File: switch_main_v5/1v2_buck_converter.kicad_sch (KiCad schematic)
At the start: 12 parts, among them U502 TPS62290TDRVRQ1

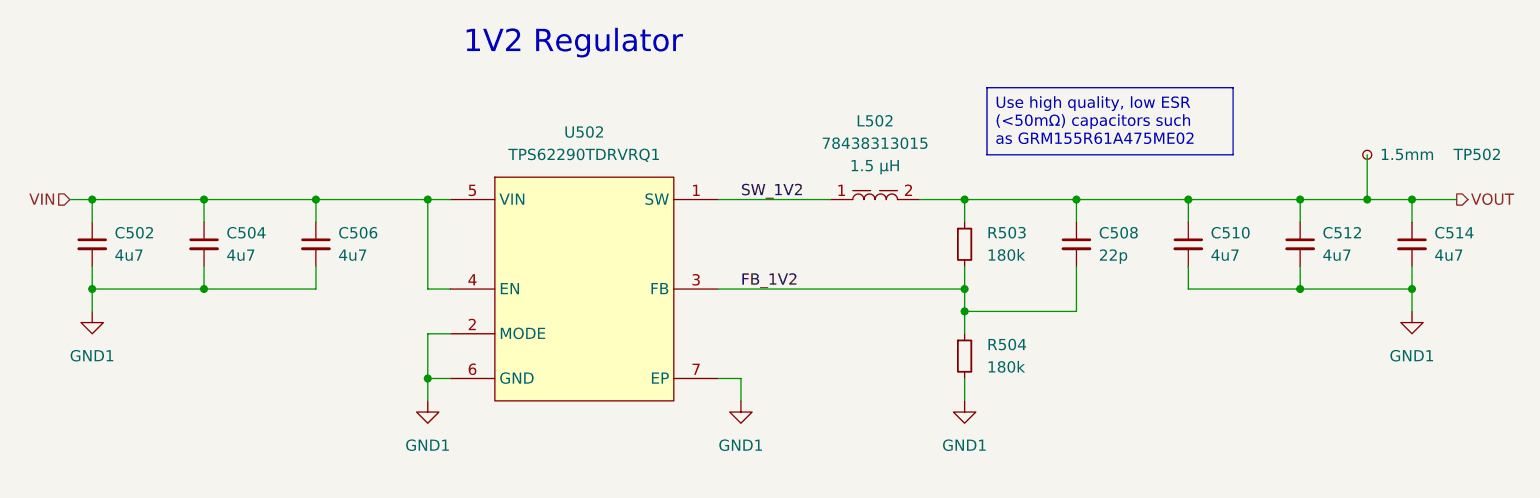
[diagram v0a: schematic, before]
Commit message: Updated 1v0_buck_converter feedback resistors
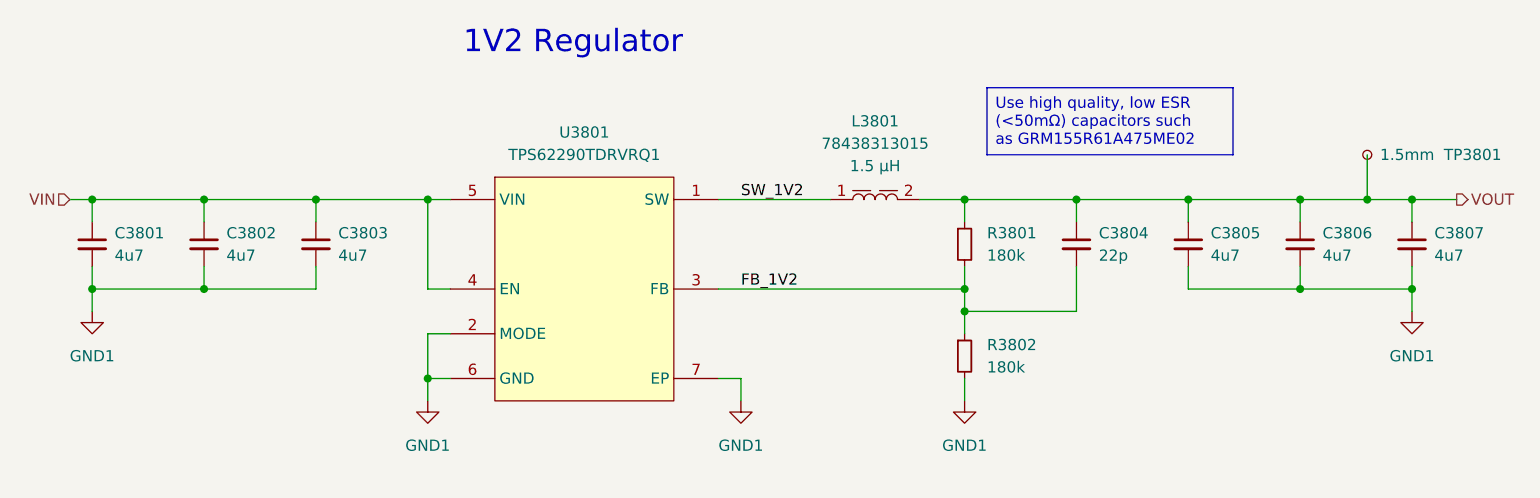
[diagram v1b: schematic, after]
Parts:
- renumbered C502 to C3801, C504 to C3802, C506 to C3803, C508 to C3804, C510 to C3805, C512 to C3806, C514 to C3807, L502 to L3801, R503 to R3801, R504 to R3802, TP502 to TP3801, U502 to U3801
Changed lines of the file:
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@@
 		(dnp no)
 		(fields_autoplaced yes)
-		(property "Reference" "C514"
+		(property "Reference" "C3807"
 			(at 231.14 95.2562 0)
 			(effects
@@
 			(project "switch_main_v5"
 				(path "/a5e57332-4284-4d3c-ab3c-13bc0ddb29b6/b1ff42f5-7cae-489e-9f8e-588cc93f3151/d017dddd-15df-4565-b589-89c8c78bc85c/6657ff67-3bc7-4183-a1c6-8c924b0e6f33"
-					(reference "C514")
+					(reference "C3807")
 					(unit 1)
 				)
@@
 		(dnp no)
 		(fields_autoplaced yes)
-		(property "Reference" "#PWR0514"
+		(property "Reference" "#PWR03805"
 			(at 228.6 110.49 0)
 			(effects
@@
 			(project "switch_main_v5"
 				(path "/a5e57332-4284-4d3c-ab3c-13bc0ddb29b6/b1ff42f5-7cae-489e-9f8e-588cc93f3151/d017dddd-15df-4565-b589-89c8c78bc85c/6657ff67-3bc7-4183-a1c6-8c924b0e6f33"
-					(reference "#PWR0514")
+					(reference "#PWR03805")
 					(unit 1)
 				)
@@
 		(dnp no)
 		(fields_autoplaced yes)
-		(property "Reference" "R504"
+		(property "Reference" "R3802"
 			(at 180.34 107.9499 0)
 			(effects
@@
 			(project "switch_main_v5"
 				(path "/a5e57332-4284-4d3c-ab3c-13bc0ddb29b6/b1ff42f5-7cae-489e-9f8e-588cc93f3151/d017dddd-15df-4565-b589-89c8c78bc85c/6657ff67-3bc7-4183-a1c6-8c924b0e6f33"
-					(reference "R504")
+					(reference "R3802")
 					(unit 1)
 				)
@@
 		(dnp no)
 		(fields_autoplaced yes)
-		(property "Reference" "C510"
+		(property "Reference" "C3805"
 			(at 205.74 95.2562 0)
 			(effects
@@
 			(project "switch_main_v5"
 				(path "/a5e57332-4284-4d3c-ab3c-13bc0ddb29b6/b1ff42f5-7cae-489e-9f8e-588cc93f3151/d017dddd-15df-4565-b589-89c8c78bc85c/6657ff67-3bc7-4183-a1c6-8c924b0e6f33"
-					(reference "C510")
+					(reference "C3805")
 					(unit 1)
 				)
@@
 		(dnp no)
 		(fields_autoplaced yes)
-		(property "Reference" "#PWR0506"
+		(property "Reference" "#PWR03802"
 			(at 116.84 120.65 0)
 			(effects
@@
 			(project "switch_main_v5"
 				(path "/a5e57332-4284-4d3c-ab3c-13bc0ddb29b6/b1ff42f5-7cae-489e-9f8e-588cc93f3151/d017dddd-15df-4565-b589-89c8c78bc85c/6657ff67-3bc7-4183-a1c6-8c924b0e6f33"
-					(reference "#PWR0506")
+					(reference "#PWR03802")
 					(unit 1)
 				)
@@
 		(on_board yes)
 		(dnp no)
-		(property "Reference" "C502"
+		(property "Reference" "C3801"
 			(at 81.28 95.2562 0)
 			(effects
@@
 			(project "switch_main_v5"
 				(path "/a5e57332-4284-4d3c-ab3c-13bc0ddb29b6/b1ff42f5-7cae-489e-9f8e-588cc93f3151/d017dddd-15df-4565-b589-89c8c78bc85c/6657ff67-3bc7-4183-a1c6-8c924b0e6f33"
-					(reference "C502")
+					(reference "C3801")
 					(unit 1)
 				)
@@
 		(on_board yes)
 		(dnp no)
-		(property "Reference" "C506"
+		(property "Reference" "C3803"
 			(at 106.68 95.2562 0)
 			(effects
@@
 			(project "switch_main_v5"
 				(path "/a5e57332-4284-4d3c-ab3c-13bc0ddb29b6/b1ff42f5-7cae-489e-9f8e-588cc93f3151/d017dddd-15df-4565-b589-89c8c78bc85c/6657ff67-3bc7-4183-a1c6-8c924b0e6f33"
-					(reference "C506")
+					(reference "C3803")
 					(unit 1)
 				)
@@
 		(dnp no)
 		(fields_autoplaced yes)
-		(property "Reference" "#PWR0510"
+		(property "Reference" "#PWR03804"
 			(at 177.8 120.65 0)
 			(effects
@@
 			(project "switch_main_v5"
 				(path "/a5e57332-4284-4d3c-ab3c-13bc0ddb29b6/b1ff42f5-7cae-489e-9f8e-588cc93f3151/d017dddd-15df-4565-b589-89c8c78bc85c/6657ff67-3bc7-4183-a1c6-8c924b0e6f33"
-					(reference "#PWR0510")
+					(reference "#PWR03804")
 					(unit 1)
 				)
@@
 		(on_board yes)
 		(dnp no)
-		(property "Reference" "C508"
+		(property "Reference" "C3804"
 			(at 193.04 95.2562 0)
 			(effects
@@
 			(project "switch_main_v5"
 				(path "/a5e57332-4284-4d3c-ab3c-13bc0ddb29b6/b1ff42f5-7cae-489e-9f8e-588cc93f3151/d017dddd-15df-4565-b589-89c8c78bc85c/6657ff67-3bc7-4183-a1c6-8c924b0e6f33"
-					(reference "C508")
+					(reference "C3804")
 					(unit 1)
 				)
@@
 		(dnp no)
 		(fields_autoplaced yes)
-		(property "Reference" "R503"
+		(property "Reference" "R3801"
 			(at 180.34 95.2499 0)
 			(effects
@@
 			(project "switch_main_v5"
 				(path "/a5e57332-4284-4d3c-ab3c-13bc0ddb29b6/b1ff42f5-7cae-489e-9f8e-588cc93f3151/d017dddd-15df-4565-b589-89c8c78bc85c/6657ff67-3bc7-4183-a1c6-8c924b0e6f33"
-					(reference "R503")
+					(reference "R3801")
 					(unit 1)
 				)
@@
 		(dnp no)
 		(fields_autoplaced yes)
-		(property "Reference" "C512"
+		(property "Reference" "C3806"
 			(at 218.44 95.2562 0)
 			(effects
@@
 			(project "switch_main_v5"
 				(path "/a5e57332-4284-4d3c-ab3c-13bc0ddb29b6/b1ff42f5-7cae-489e-9f8e-588cc93f3151/d017dddd-15df-4565-b589-89c8c78bc85c/6657ff67-3bc7-4183-a1c6-8c924b0e6f33"
-					(reference "C512")
+					(reference "C3806")
 					(unit 1)
 				)
@@
 		(dnp no)
 		(fields_autoplaced yes)
-		(property "Reference" "#PWR0504"
+		(property "Reference" "#PWR03801"
 			(at 78.74 110.49 0)
 			(effects
@@
 			(project "switch_main_v5"
 				(path "/a5e57332-4284-4d3c-ab3c-13bc0ddb29b6/b1ff42f5-7cae-489e-9f8e-588cc93f3151/d017dddd-15df-4565-b589-89c8c78bc85c/6657ff67-3bc7-4183-a1c6-8c924b0e6f33"
-					(reference "#PWR0504")
+					(reference "#PWR03801")
 					(unit 1)
 				)
@@
 		(dnp no)
 		(fields_autoplaced yes)
-		(property "Reference" "U502"
+		(property "Reference" "U3801"
 			(at 134.62 83.82 0)
 			(effects
@@
 			(project "switch_main_v5"
 				(path "/a5e57332-4284-4d3c-ab3c-13bc0ddb29b6/b1ff42f5-7cae-489e-9f8e-588cc93f3151/d017dddd-15df-4565-b589-89c8c78bc85c/6657ff67-3bc7-4183-a1c6-8c924b0e6f33"
-					(reference "U502")
+					(reference "U3801")
 					(unit 1)
 				)
@@
 		(dnp no)
 		(fields_autoplaced yes)
-		(property "Reference" "L502"
+		(property "Reference" "L3801"
 			(at 167.64 82.55 0)
 			(effects
@@
 			(project "switch_main_v5"
 				(path "/a5e57332-4284-4d3c-ab3c-13bc0ddb29b6/b1ff42f5-7cae-489e-9f8e-588cc93f3151/d017dddd-15df-4565-b589-89c8c78bc85c/6657ff67-3bc7-4183-a1c6-8c924b0e6f33"
-					(reference "L502")
+					(reference "L3801")
 					(unit 1)
 				)
@@
 		(dnp no)
 		(fields_autoplaced yes)
-		(property "Reference" "#PWR0508"
+		(property "Reference" "#PWR03803"
 			(at 152.4 120.65 0)
 			(effects
@@
 			(project "switch_main_v5"
 				(path "/a5e57332-4284-4d3c-ab3c-13bc0ddb29b6/b1ff42f5-7cae-489e-9f8e-588cc93f3151/d017dddd-15df-4565-b589-89c8c78bc85c/6657ff67-3bc7-4183-a1c6-8c924b0e6f33"
-					(reference "#PWR0508")
+					(reference "#PWR03803")
 					(unit 1)
 				)
@@
 		(on_board yes)
 		(dnp no)
-		(property "Reference" "C504"
+		(property "Reference" "C3802"
 			(at 93.98 95.2562 0)
 			(effects
@@
 			(project "switch_main_v5"
 				(path "/a5e57332-4284-4d3c-ab3c-13bc0ddb29b6/b1ff42f5-7cae-489e-9f8e-588cc93f3151/d017dddd-15df-4565-b589-89c8c78bc85c/6657ff67-3bc7-4183-a1c6-8c924b0e6f33"
-					(reference "C504")
+					(reference "C3802")
 					(unit 1)
 				)
@@
 		(on_board yes)
 		(dnp no)
-		(property "Reference" "TP502"
+		(property "Reference" "TP3801"
 			(at 238.76 86.36 0)
 			(effects
@@
 			(project "switch_main_v5"
 				(path "/a5e57332-4284-4d3c-ab3c-13bc0ddb29b6/b1ff42f5-7cae-489e-9f8e-588cc93f3151/d017dddd-15df-4565-b589-89c8c78bc85c/6657ff67-3bc7-4183-a1c6-8c924b0e6f33"
-					(reference "TP502")
-					(unit 1)
-				)
+					(reference "TP3801")
+					(unit 1)
+				)

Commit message: 1V0 Rail done
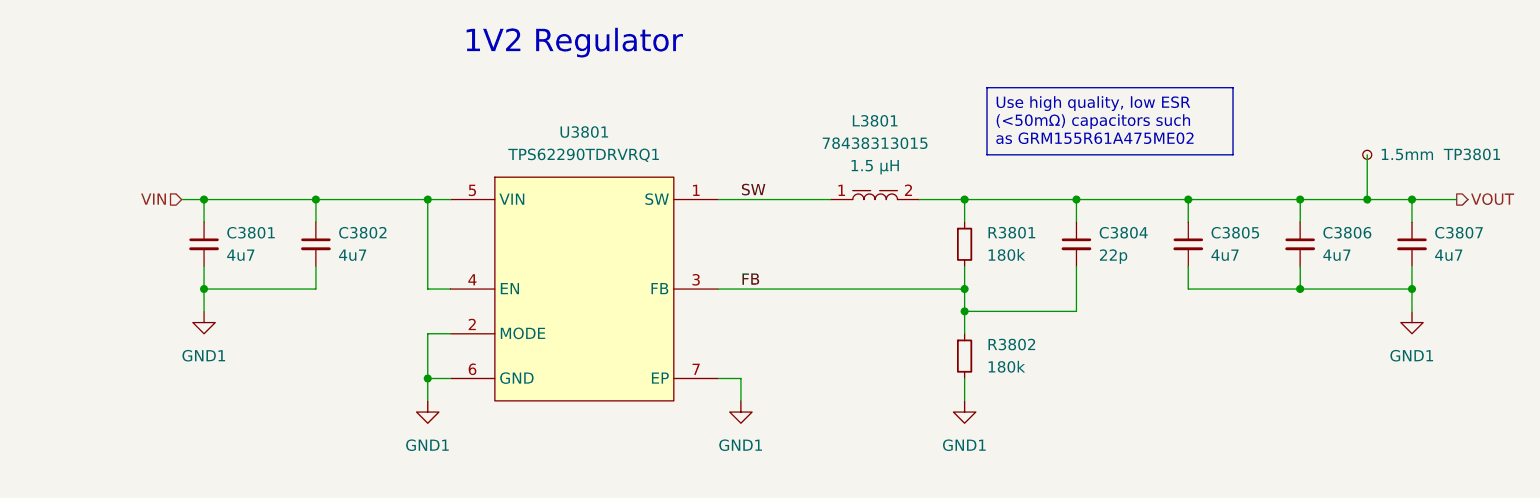
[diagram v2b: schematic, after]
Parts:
- removed C3803: 4u7, Capacitor_SMD:C_0402_1005Metric, symbol Device:C_Small
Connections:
- net FB_1V2 renamed FB
- net SW_1V2 renamed SW
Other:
- moved on the sheet: C3801, C3802

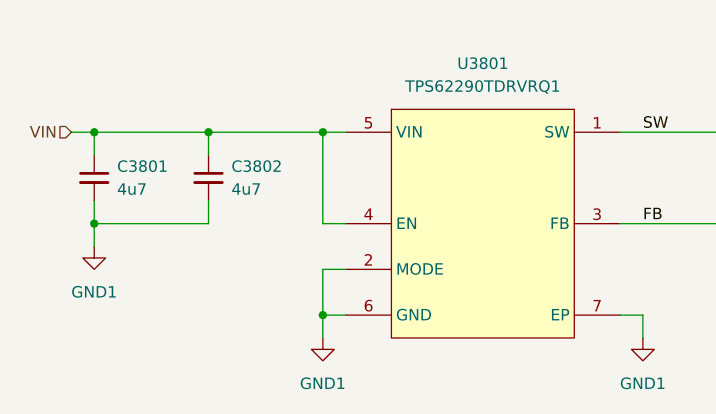
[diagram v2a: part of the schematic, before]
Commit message: Placed most remaining passives and test points
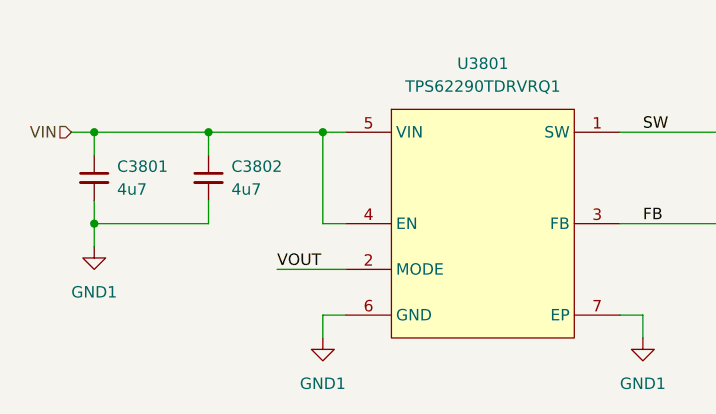
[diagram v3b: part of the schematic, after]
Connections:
- net GND1: no longer U3801.2 (MODE)
- net VOUT: now also U3801.2 (MODE)
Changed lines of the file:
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@@
-	)
-	(junction
-		(at 116.84 111.76)
-		(diameter 0)
-		(color 0 0 0 0)
 	)
 	(junction
@@
 	(wire
 		(pts
-			(xy 119.38 106.68) (xy 116.84 106.68)
-		)
-		(stroke
-			(width 0)
-			(type default)
-		)
-	)
-	(wire
-		(pts
 			(xy 116.84 91.44) (xy 119.38 91.44)
 		)
@@
 	(wire
 		(pts
-			(xy 116.84 106.68) (xy 116.84 111.76)
-		)
-		(stroke
-			(width 0)
-			(type default)
-		)
-	)
-	(wire
-		(pts
 			(xy 203.2 91.44) (xy 203.2 93.98)
 		)
@@
 	(wire
 		(pts
+			(xy 111.76 106.68) (xy 119.38 106.68)
+		)
+		(stroke
+			(width 0)
+			(type default)
+		)
+	)
+	(wire
+		(pts
 			(xy 223.52 86.36) (xy 223.52 91.44)
 		)
@@
 		)
 	)
+	(label "VOUT"
+		(at 111.76 106.68 0)
+		(effects
+			(font
+				(size 1.27 1.27)
+			)
+			(justify left bottom)
+		)
+	)

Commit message: Tidied schematic and PCB
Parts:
- renumbered C3801 to C801, C3802 to C802, C3804 to C803, C3805 to C804, C3806 to C805, C3807 to C806, L3801 to L801, R3801 to R801, R3802 to R802, TP3801 to TP801, U3801 to U801
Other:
- moved on the sheet: C801, C802, C803, C804, C805, C806, L801, R801, R802, TP801, U801
